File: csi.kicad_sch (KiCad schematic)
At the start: 61 parts, among them J10 Conn_FFC_WE_68715014522, J11 Conn_FFC_WE_68715014522, U43 PI4MSD5V9548AZDEX, U44 AP22615A_TSOT26, U45 AP22615A_TSOT26, U46 AP22615A_TSOT26, U47 AP22615A_TSOT26, U48 NTS0102_XSON, U49 NTS0102_XSON

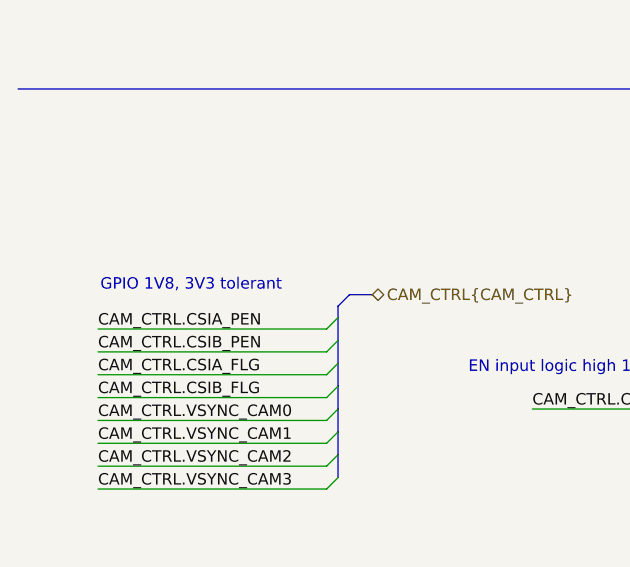
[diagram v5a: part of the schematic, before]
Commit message: [#85326] Fix incorrect GPIO voltage levels, add SFP related TVS
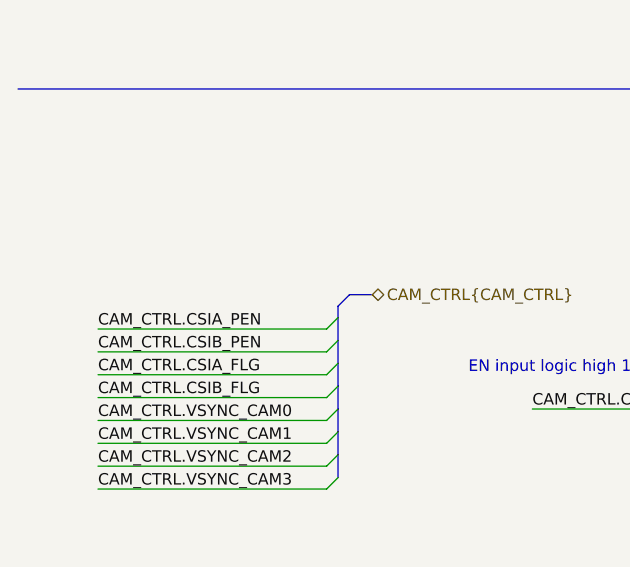
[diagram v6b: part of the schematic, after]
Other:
- note removed: "GPIO 1V8, 3V3 tolerant"
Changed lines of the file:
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@@
 		)
 	)
-	(text "GPIO 1V8, 3V3 tolerant"
-		(exclude_from_sim no)
-		(at 21.844 202.184 0)
-		(effects
-			(font
-				(size 1.27 1.27)
-			)
-			(justify left)
-		)
-	)
 	(text "CSI2 x2"
 		(exclude_from_sim no)
@@
 		(polyline
 			(pts
-				(xy 279.4 105.41) (xy 267.97 105.41) (xy 267.97 30.48) (xy 279.4 30.48)
+				(xy 356.87 105.41) (xy 345.44 105.41) (xy 345.44 30.48) (xy 356.87 30.48)
 			)
 			(stroke
@@
 		(polyline
 			(pts
-				(xy 356.87 105.41) (xy 345.44 105.41) (xy 345.44 30.48) (xy 356.87 30.48)
+				(xy 279.4 105.41) (xy 267.97 105.41) (xy 267.97 30.48) (xy 279.4 30.48)
 			)
 			(stroke

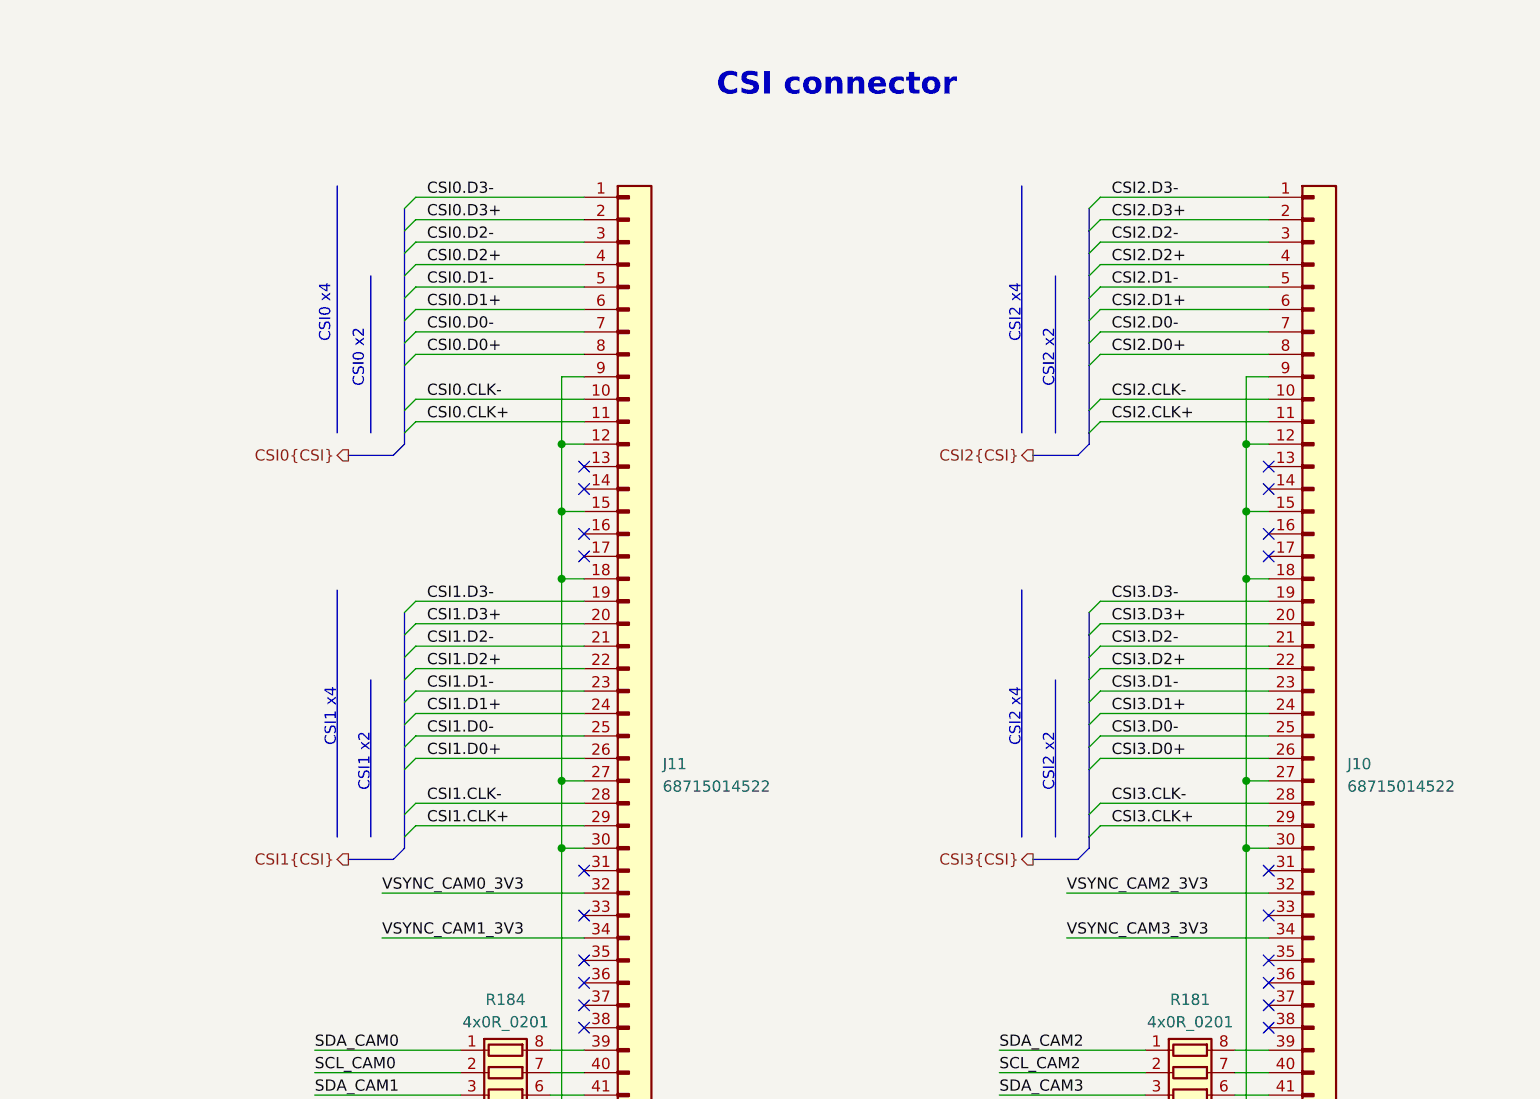
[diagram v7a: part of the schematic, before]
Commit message: [#85326] Update CSI naming convention
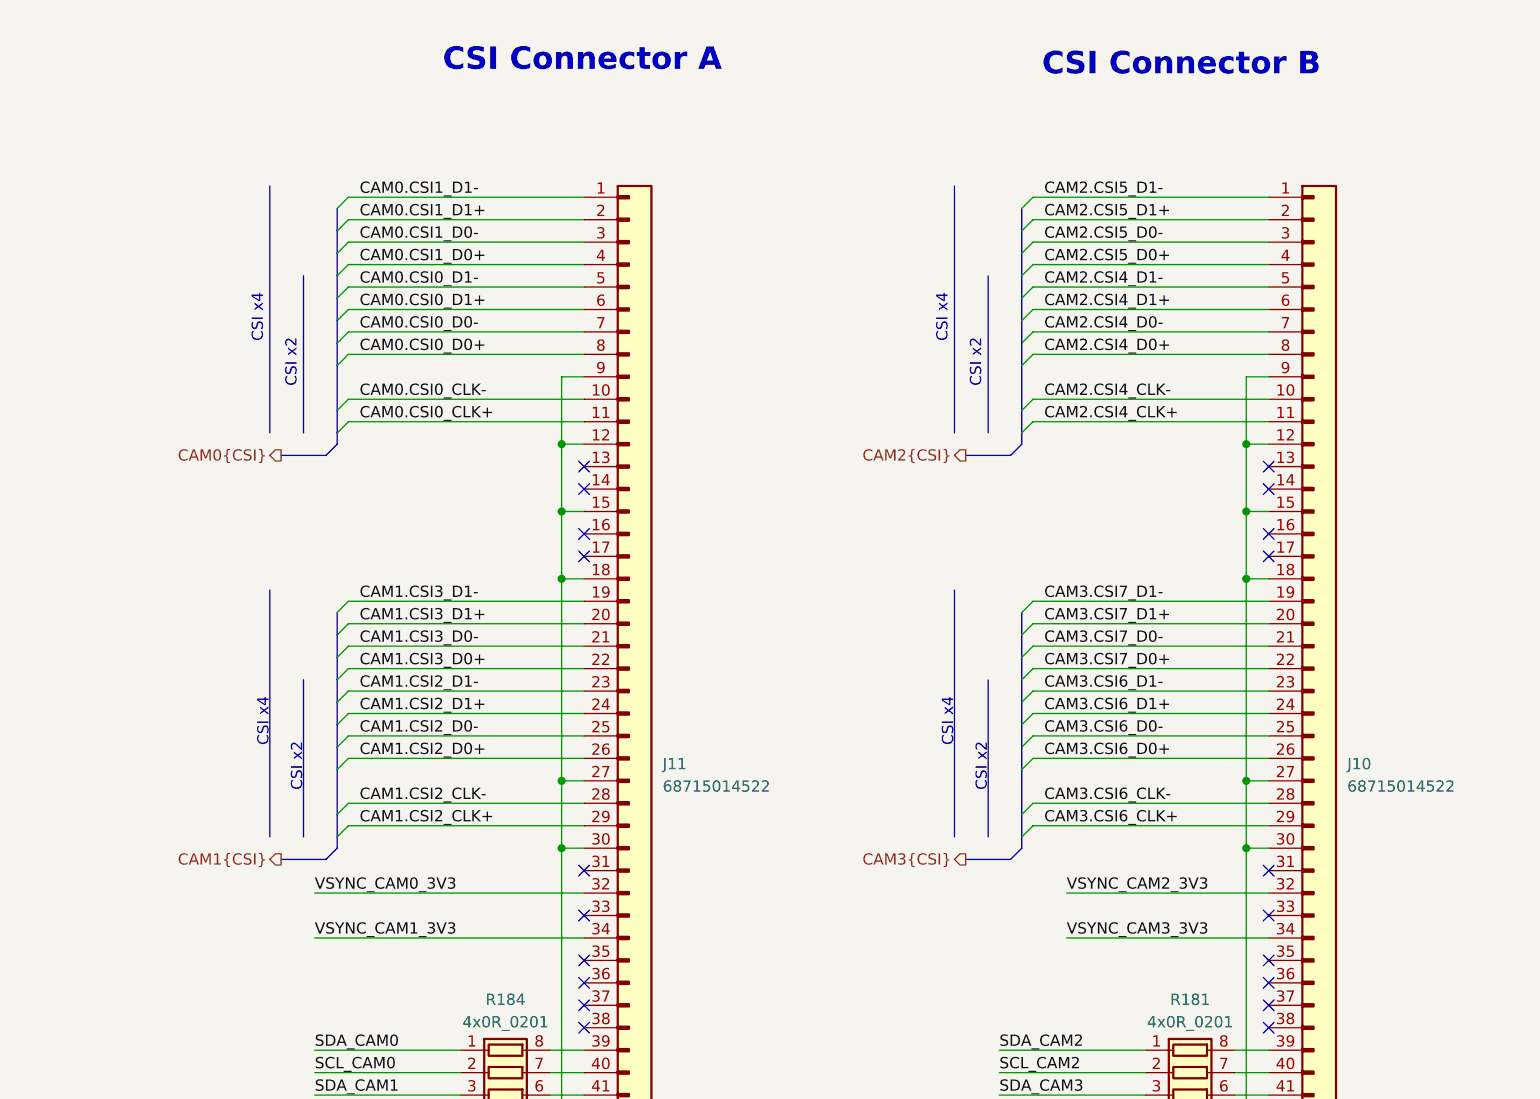
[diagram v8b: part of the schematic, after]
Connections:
- net CSI0.CLK+ renamed CAM0.CSI0_CLK+
- net CSI0.CLK- renamed CAM0.CSI0_CLK-
- net CSI0.D0+ renamed CAM0.CSI0_D0+
- net CSI0.D0- renamed CAM0.CSI0_D0-
- net CSI0.D1+ renamed CAM0.CSI0_D1+
- net CSI0.D1- renamed CAM0.CSI0_D1-
- net CSI0.D2+ renamed CAM0.CSI1_D0+
- net CSI0.D2- renamed CAM0.CSI1_D0-
- net CSI0.D3+ renamed CAM0.CSI1_D1+
- net CSI0.D3- renamed CAM0.CSI1_D1-
- net CSI1.CLK+ renamed CAM1.CSI2_CLK+
- net CSI1.CLK- renamed CAM1.CSI2_CLK-
- net CSI1.D0+ renamed CAM1.CSI2_D0+
- net CSI1.D0- renamed CAM1.CSI2_D0-
- net CSI1.D1+ renamed CAM1.CSI2_D1+
- net CSI1.D1- renamed CAM1.CSI2_D1-
- net CSI1.D2+ renamed CAM1.CSI3_D0+
- net CSI1.D2- renamed CAM1.CSI3_D0-
- net CSI1.D3+ renamed CAM1.CSI3_D1+
- net CSI1.D3- renamed CAM1.CSI3_D1-
- net CSI2.CLK+ renamed CAM2.CSI4_CLK+
- net CSI2.CLK- renamed CAM2.CSI4_CLK-
- net CSI2.D0+ renamed CAM2.CSI4_D0+
- net CSI2.D0- renamed CAM2.CSI4_D0-
- net CSI2.D1+ renamed CAM2.CSI4_D1+
- net CSI2.D1- renamed CAM2.CSI4_D1-
- net CSI2.D2+ renamed CAM2.CSI5_D0+
- net CSI2.D2- renamed CAM2.CSI5_D0-
- net CSI2.D3+ renamed CAM2.CSI5_D1+
- net CSI2.D3- renamed CAM2.CSI5_D1-
- net CSI3.CLK+ renamed CAM3.CSI6_CLK+
- net CSI3.CLK- renamed CAM3.CSI6_CLK-
- net CSI3.D0+ renamed CAM3.CSI6_D0+
- net CSI3.D0- renamed CAM3.CSI6_D0-
- net CSI3.D1+ renamed CAM3.CSI6_D1+
- net CSI3.D1- renamed CAM3.CSI6_D1-
- net CSI3.D2+ renamed CAM3.CSI7_D0+
- net CSI3.D2- renamed CAM3.CSI7_D0-
- net CSI3.D3+ renamed CAM3.CSI7_D1+
- net CSI3.D3- renamed CAM3.CSI7_D1-
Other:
- note added: "CSI Connector A"
- note added: "CSI Connector B"
- note added: "CSI x2"
- note added: "CSI x4"
- note removed: "CSI connector"
- note removed: "CSI0 x2"
- note removed: "CSI0 x4"
- note removed: "CSI1 x2"
- note removed: "CSI1 x4"
- note removed: "CSI2 x2"
- note removed: "CSI2 x4"
